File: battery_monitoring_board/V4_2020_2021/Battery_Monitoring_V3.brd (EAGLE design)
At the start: 57.1 x 161.5 mm, 97 parts, among them CON1 MOLEX_5566-2, CON2 SM03B-GHS-TB, CON3 SM03B-GHS-TB, J1 MKDS_5/2-6,352, J10 MKDS_5/2-6,352, J11 MKDS_5/2-6,352, J2 MKDS_5/2-6,352, J3 MKDS_5/2-6,352, J4 MKDS_5/2-6,352, J5 MKDS_5/2-6,352, J6 MKDS_5/2-6,352, J7 MKDS_5/2-6,352, J8 MKDS_5/2-6,352, J9 MKDS_5/2-6,352, Q1 TCLD1000CT, Q10 SI7145DP, Q11 SI7145DP, Q12 SI7145DP, Q13 SI7145DP, Q14 SI7145DP, Q15 PSMN1R5-30BLE, Q16 TCLD1000CT, Q2 TCLD1000CT, Q3 TCLD1000CT, Q4 PSMN1R5-30BLE, Q5 PSMN1R5-30BLE, Q6 PSMN1R5-30BLE, Q7 SI7145DP, Q8 SI7145DP, Q9 SI7145DP, U1 INA3221., U2 INA3221., U3 TEENSY_3.1_BASIC_2, U4 TCAN1042HVDR, U5 LTC4418

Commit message: started new sheet
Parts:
- added 3V3, DANGER: (no value), adafruit:1206
- added C13, C14, C15, C16: 0.01uF, adafruit:C0805
- added C17: 10uF, adafruit:C1206
- added C18: 1.5uF, adafruit:C0805
- added CON4: MOLEX_5566-2, ARVP:5566-2
- added D5: (no value), diode:DO-214AC
- added J12, J13, J14, J15, J16, J17: MKDS_5/2-6,352, Moira:MKDS_5/2-6,35
- added JP7: (no value), pinhead:1X02
- added Q17, Q18, Q19, Q20: NMOS-TO252, AlbertaSat:TO252
- added Q21: DMN2011UTS, Lydia:SOP65P640X120-8N
- added R39, R40: 240, resistor:R1206
- added R41, R42, R43, R44: 100k, adafruit:R1206
- added R45: 5.1, adafruit:R1206
- added R46: 1k, rcl:R0805
- added U10, U6, U7, U8: LM5050-2, AlbertaSat:MK06A
- added U12: IR2301S, Lydia:SOIC8
- added U9: TEENSY_3.1_BASIC_2, Teensy_3_Series_Board_v1.0:TEENSY_3.1_BASIC_2
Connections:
- new net +5V1: JP7.2
- new net GATE1: Q17.1, U6.5
- new net GATE2: Q18.1, U7.5
- new net GATE3: Q19.1, U8.5
- new net GATE4: Q20.1, U10.5
- new net GATE5: R46.1, U12.7
- new net IO1: U12.2, U9.10
- new net IO2: U10.3, U6.3, U7.3, U8.3, U9.6
- new net IO3: R42.1, U7.1, U9.8
- new net IO4: R41.1, U8.1, U9.5
- new net IO5: R43.1, U6.1, U9.9
- new net IO6: R44.1, U10.1, U9.7
- new net LEAK_IN: U9.14/A0
- new net LED_D: R39.1, U9.23/A9
- new net N$12: DANGER.A, R39.2
- new net N$13: C17.1, J15.2, Q21.5, Q21.6, Q21.7, Q21.8, R45.1, U12.1
- new net N$17: 3V3.A, R40.1
- new net N$18: C18.2, U12.6
- new net N$19: C18.1, D5.C, U12.8
- new net N$20: Q21.4, R46.2
- new net N$21: D5.A, R45.2
- new net VBATT1: C14.1, J14.2, Q17.3, U6.4
- new net VBATT2: C13.1, J13.2, Q18.3, U7.4
- new net VBATT3: C15.1, J12.2, Q19.3, U8.4
- new net VBATT4: C16.1, J17.2, Q20.3, U10.4
- new net VIN1: JP7.1
- new net VOUT: J16.1, Q17.2, Q18.2, Q19.2, Q20.2, Q21.1, Q21.2, Q21.3, U10.6, U6.6, U7.6, U8.6
- net +3V3: now also R40.2, U9.3.3V
- net +5V: now also CON4.1, R41.2, R42.2, R43.2, R44.2
- net AGND: now also U9.AGND
- net GND: now also 3V3.C, C13.2, C14.2, C15.2, C16.2, C17.2, CON4.2, DANGER.C, J12.1, J13.1, J14.1, J15.1, J16.2, J17.1, U10.2, U12.3, U12.4, U6.2, U7.2, U8.2, U9.GND
- net VIN: now also U9.VIN

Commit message: Removed duplicate teensy
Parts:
- removed 3V3, DANGER: (no value), adafruit:1206
- removed CON4: MOLEX_5566-2, ARVP:5566-2
- removed JP7: (no value), pinhead:1X02
- removed R39, R40: 240, resistor:R1206
- removed U9: TEENSY_3.1_BASIC_2, Teensy_3_Series_Board_v1.0:TEENSY_3.1_BASIC_2
- added 3V1, DANGER1: (no value), adafruit:1206
- added R36, R37: 240, resistor:R1206
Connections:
- removed net +5V1: JP7.2
- removed net N$12: DANGER.A, R39.2
- removed net N$17: 3V3.A, R40.1
- removed net VIN1: JP7.1
- new net N$22: 3V1.A, R37.1
- new net N$23: DANGER1.A, R36.2
- net +3V3: now also R37.2; no longer R40.2, U9.3.3V
- net +5V: no longer CON4.1
- net AGND: no longer U9.AGND
- net GND: now also 3V1.C, DANGER1.C; no longer 3V3.C, CON4.2, DANGER.C, U9.GND
- net IO1: now also U3.17/A3; no longer U9.10
- net IO2: now also U3.13; no longer U9.6
- net IO3: now also U3.15/A1; no longer U9.8
- net IO4: now also U3.12; no longer U9.5
- net IO5: now also U3.16/A2; no longer U9.9
- net IO6: now also U3.14/A0; no longer U9.7
- net LEAK_IN: now also U3.11; no longer U9.14/A0
- net LED_D: now also R36.1, U3.23/A9; no longer R39.1, U9.23/A9
- net VIN: no longer U9.VIN

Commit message: Removed jumpers
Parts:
- removed J11, J12, J13, J14, J15, J17, J5, J6, J7, J8: MKDS_5/2-6,352, Moira:MKDS_5/2-6,35
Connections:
- removed net LEAK_IN: U3.11
- removed net N$13: C17.1, J15.2, Q21.5, Q21.6, Q21.7, Q21.8, R45.1, U12.1
- removed net VBATT1: C14.1, J14.2, Q17.3, U6.4
- removed net VBATT2: C13.1, J13.2, Q18.3, U7.4
- removed net VBATT3: C15.1, J12.2, Q19.3, U8.4
- removed net VBATT4: C16.1, J17.2, Q20.3, U10.4
- net ELECTRONICS_BATTERY: now also C17.1, Q21.5, Q21.6, Q21.7, Q21.8, R45.1, U12.1
- net GND: no longer J11.2, J12.1, J13.1, J14.1, J15.1, J17.1, J5.2, J6.2, J7.2, J8.2
- net MOTOR1: now also C14.1, Q17.3, U6.4; no longer J5.1
- net MOTOR2: now also C13.1, Q18.3, U7.4; no longer J6.1
- net MOTOR3: now also C15.1, Q19.3, U8.4; no longer J7.1
- net MOTOR4: now also C16.1, Q20.3, U10.4; no longer J11.1
- net POWER_BOARD: no longer J8.1
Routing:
- net MOTOR4: track 127.8 -> 121.9 mm

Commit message: started work on PCB layout
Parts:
- moved Q17 129.3 mm to (-15.0, 65.4), turned to 270 degrees
- moved Q19 124.6 mm to (8.76, 60.8), turned to 270 degrees
- moved Q18 111.7 mm to (9.27, 48.9), turned to 270 degrees
- moved Q20 106.1 mm to (-15.6, 30.1), turned to 270 degrees
- moved J16 77.4 mm to (-16.8, 15.5), turned to 270 degrees
- moved C13 49.7 mm to (37.6, -32.8)
- moved C14 49.7 mm to (44.8, -32.8)
- moved C15 49.7 mm to (52.1, -32.8)
- moved C16 49.7 mm to (59.3, -32.8)
- moved C18 49.7 mm to (-0.13, -39.0)
- moved R36 49.7 mm to (0.25, -63.0)
- moved R37 49.7 mm to (5.33, -63.0)
- moved R46 49.7 mm to (45.1, -22.2)
- moved U10 49.7 mm to (52.5, -38.9)
- moved U6 49.7 mm to (34.5, -38.9)
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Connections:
- net ELECTRONICS_BATTERY: no longer C17.1, Q21.5, Q21.6, Q21.7, Q21.8, R45.1, U12.1
- net POWER_BOARD: now also C17.1, Q21.5, Q21.6, Q21.7, Q21.8, R45.1, U12.1
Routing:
- net MOTOR2: track 121.2 -> 93.3 mm
- net MOTOR3: track 107.7 -> 104.1 mm
- net BATTERY_3: track 149.7 -> 147.0 mm
- net BATTERY_2: track 128.0 -> 127.4 mm

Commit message: slight positioning changes
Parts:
- moved Q17 33.0 mm to (9.27, 43.0)
- moved Q20 25.4 mm to (9.65, 27.6)
- moved Q7 12.3 mm to (33.3, 57.3)
- moved Q9 12.1 mm to (32.4, 43.2)
- moved R8 12.0 mm to (22.2, 43.1)
- moved R35 10.6 mm to (22.2, 27.7)
- moved C2 8.81 mm to (17.1, 135.2)
- moved ARVP1 8.81 mm to (9.53, 109.8)
- moved C1 8.81 mm to (15.9, 145.3)
- moved C10 8.81 mm to (3.17, 100.9)
- moved C3 8.81 mm to (43.5, 139.5)
- moved C4 8.81 mm to (36.4, 143.4)
- moved C5 8.81 mm to (13.3, 92.0)
- moved C6 8.81 mm to (8.26, 92.0)
- moved C7 8.81 mm to (4.45, 92.0)
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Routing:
- net BATTERY_4: track 173.6 -> 138.1 mm
- net MOTOR1: track 143.0 -> 116.7 mm
- net BATTERY_5: track 146.4 -> 135.8 mm
- net N$6: track 10.9 -> 2.86 mm
- net +3V3: track 123.6 -> 118.2 mm
- net SDA: track 80.4 -> 75.9 mm
- net SCL: track 69.3 -> 64.8 mm
- net MOTOR4: track 121.9 -> 120.5 mm
- net N$9: track 10.9 -> 9.55 mm

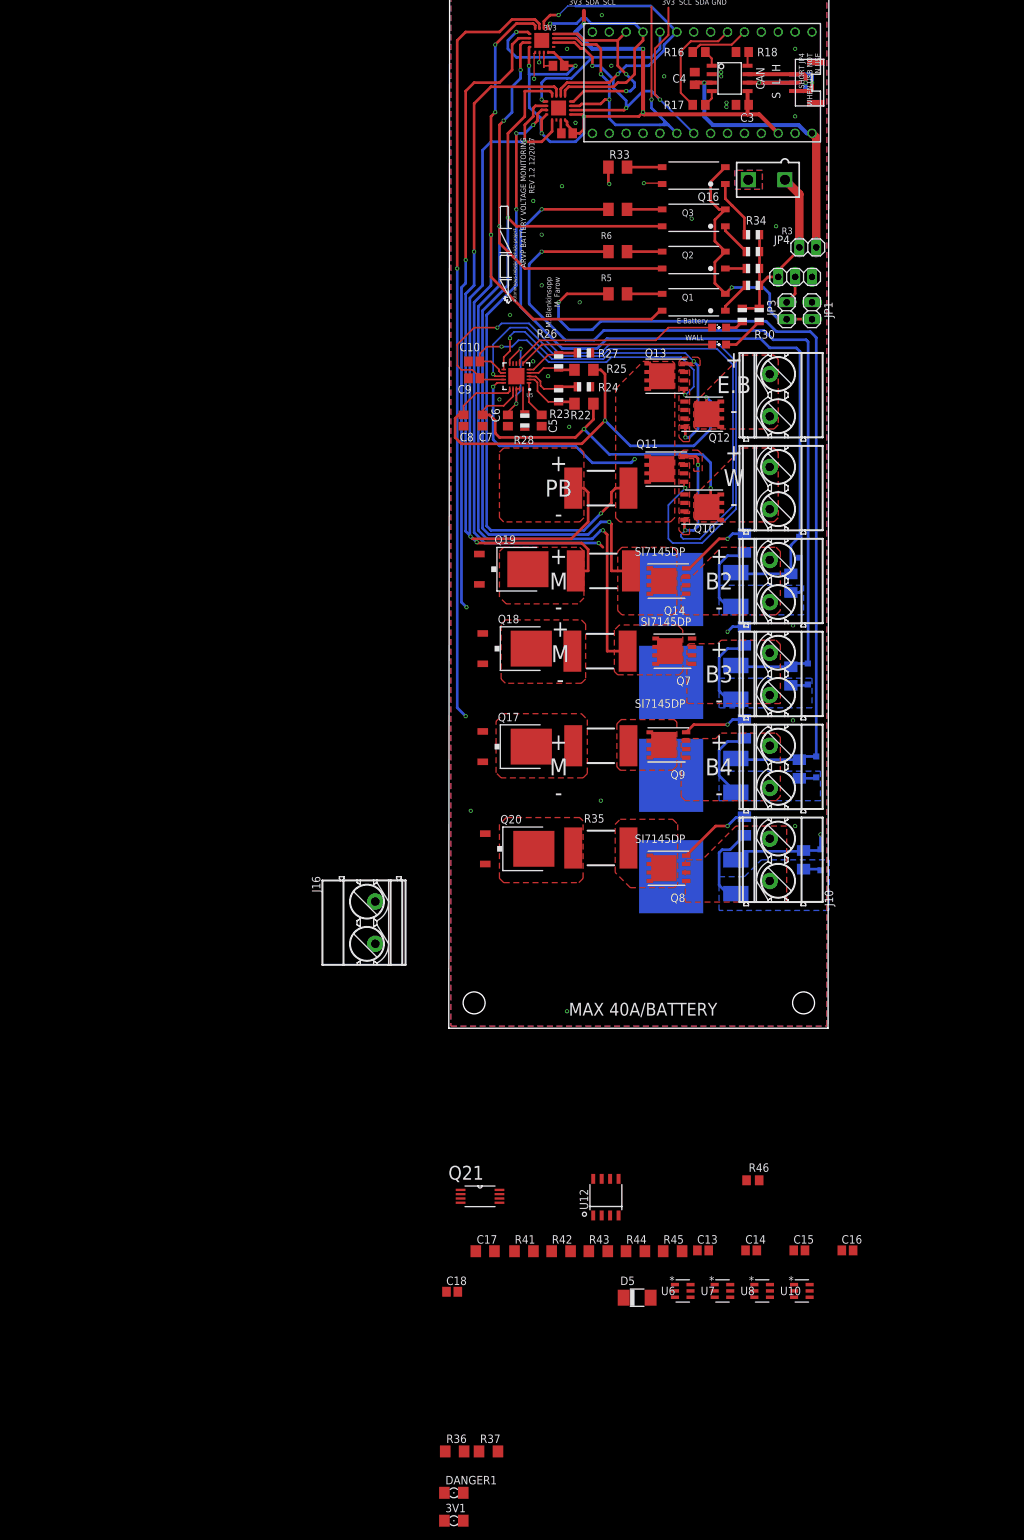
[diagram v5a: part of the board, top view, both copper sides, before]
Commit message: adjusting the resistor, capacitor, and ic positions
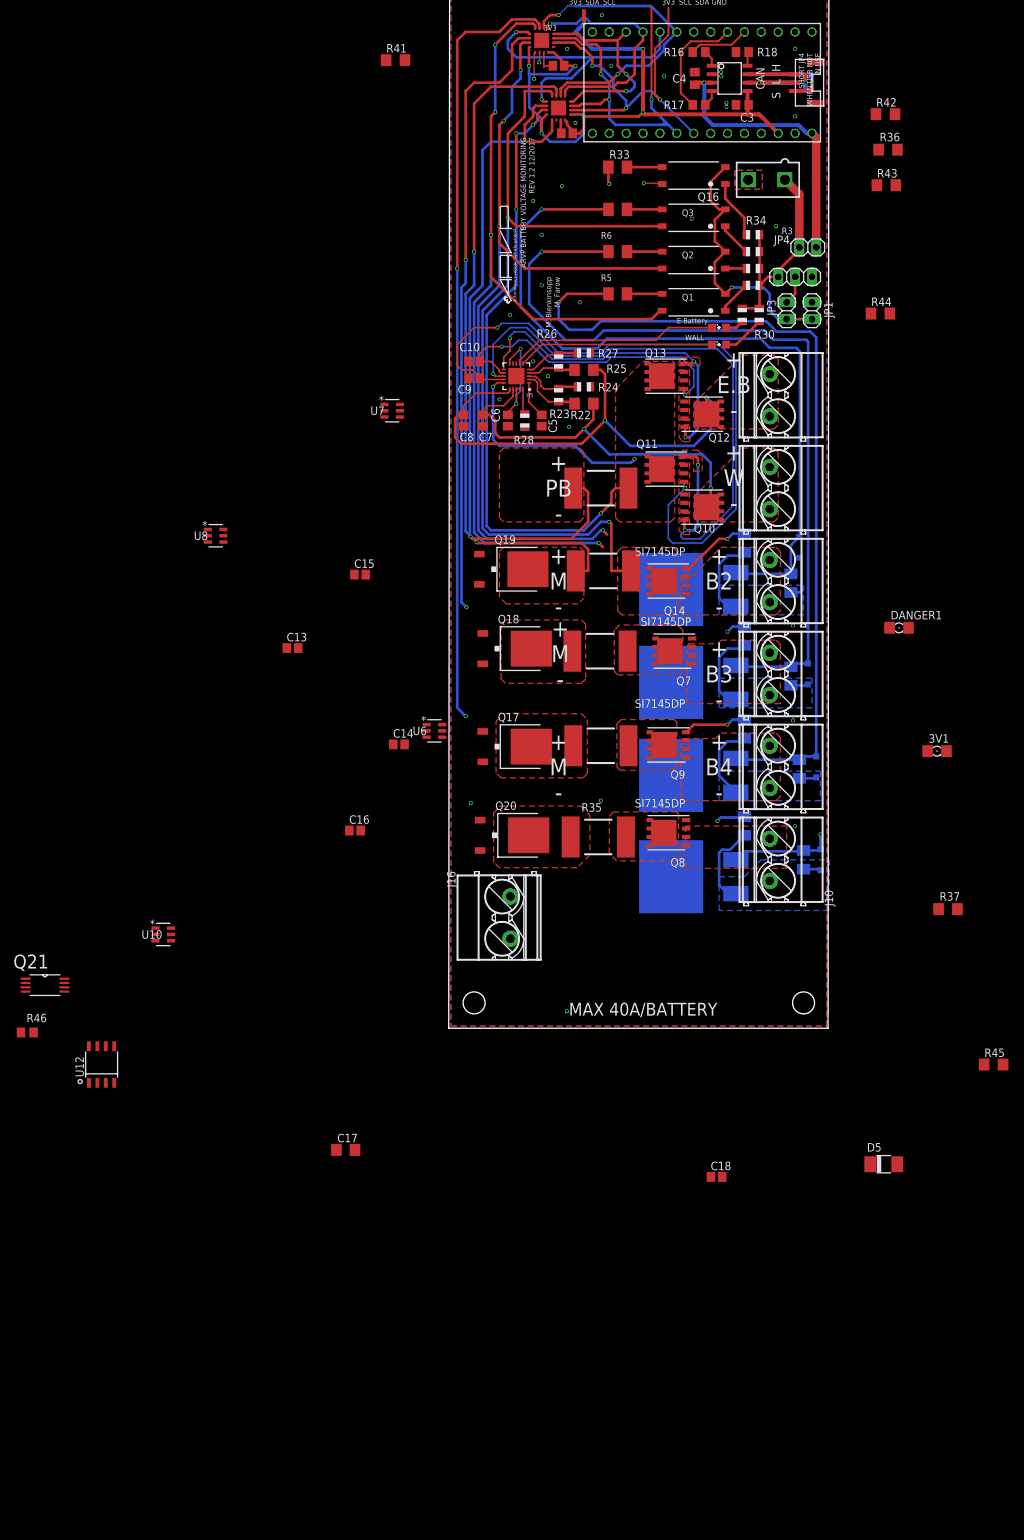
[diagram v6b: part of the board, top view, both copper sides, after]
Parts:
- moved R36 206.3 mm to (65.4, 132.7)
- moved R41 180.1 mm to (-8.64, 146.2)
- moved R42 177.8 mm to (65.0, 138.0)
- moved R43 166.0 mm to (65.2, 127.4)
- moved DANGER1 146.3 mm to (67.1, 60.8)
- moved R44 145.7 mm to (64.3, 108.1)
- moved U7 141.3 mm to (-9.14, 93.5)
- moved U8 140.2 mm to (-35.7, 74.7)
- moved 3V1 136.6 mm to (72.8, 42.3)
- moved C15 121.2 mm to (-14.0, 68.8)
- moved R46 111.3 mm to (-64.0, 0.00)
- moved U10 110.0 mm to (-43.6, 14.7)
- moved C13 109.6 mm to (-24.1, 57.8)
- moved R37 106.9 mm to (74.4, 18.5)
- moved C16 97.3 mm to (-14.7, 30.4)
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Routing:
- net BATTERY_3: track 147.0 -> 126.4 mm
- net N$10: track 11.1 -> 4.27 mm
- net MOTOR4: track 120.5 -> 119.4 mm

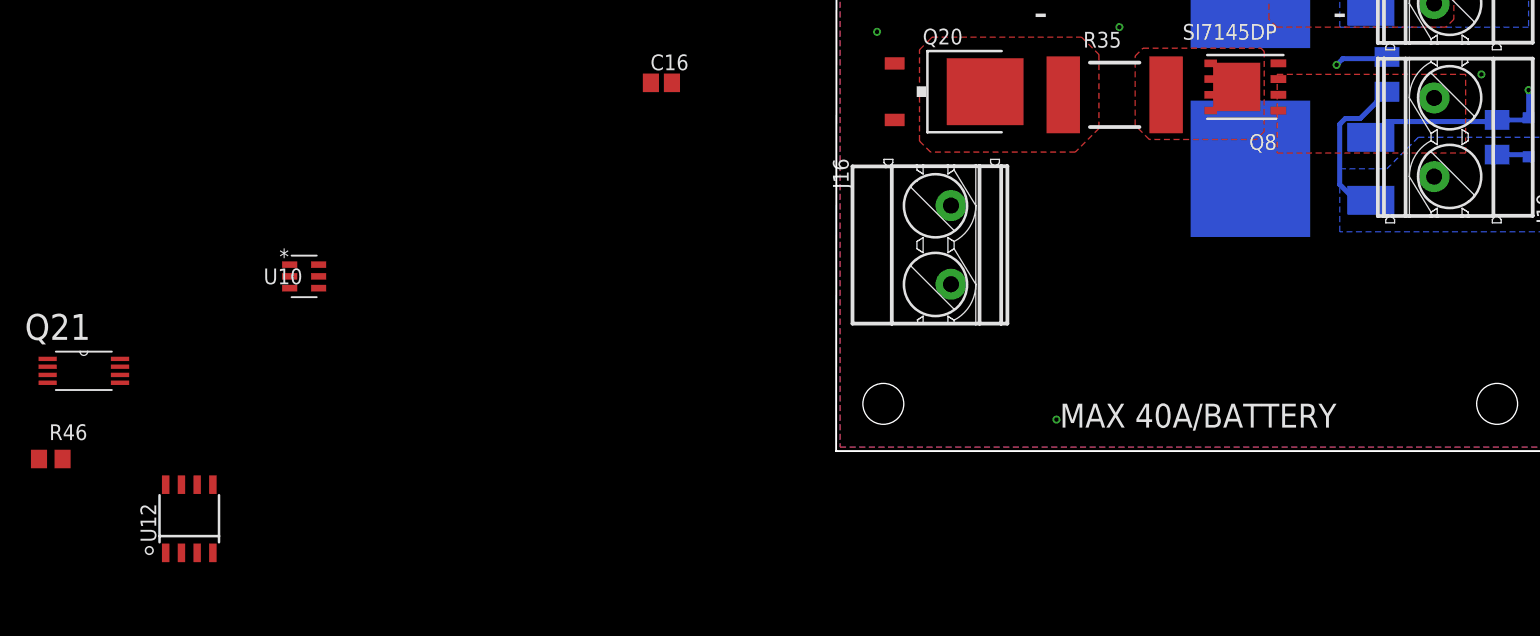
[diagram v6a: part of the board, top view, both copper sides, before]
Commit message: minor component location changes
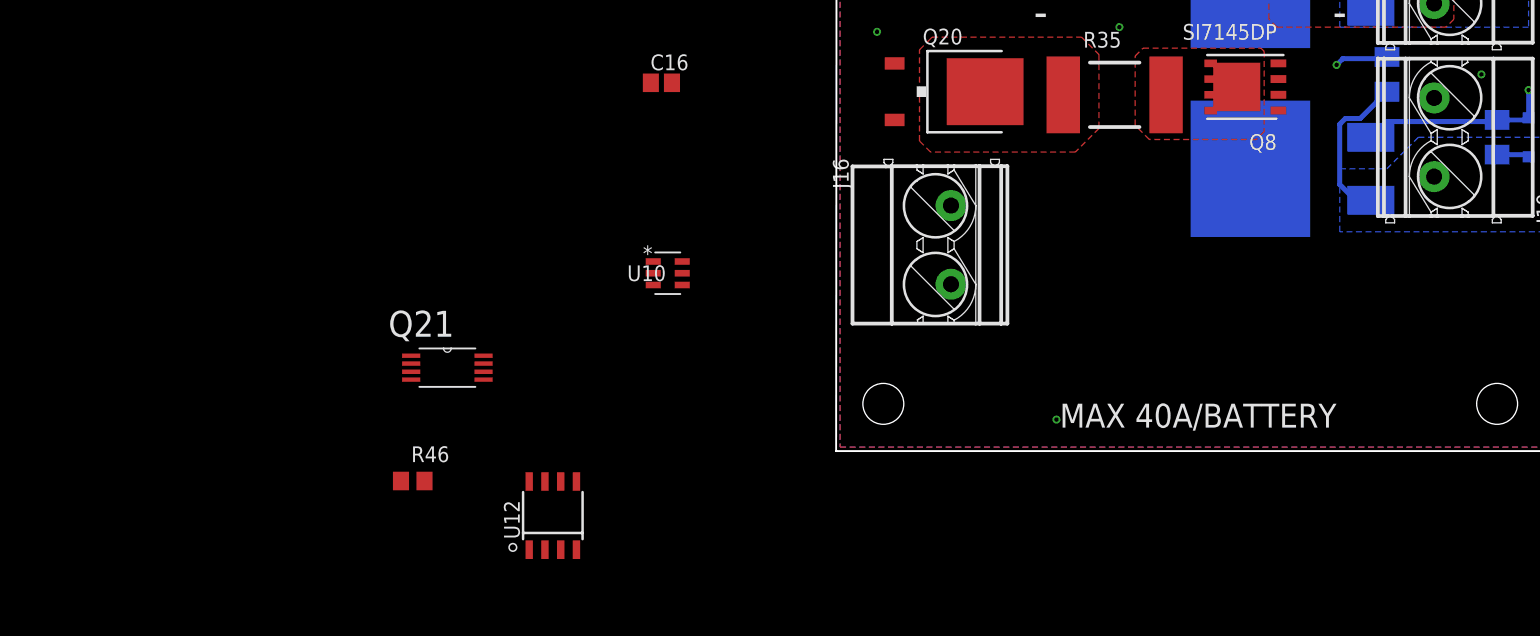
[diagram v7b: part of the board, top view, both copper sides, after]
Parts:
- moved Q21 29.3 mm to (-32.0, 7.37)
- moved U10 29.3 mm to (-14.2, 15.0)
- moved U12 29.3 mm to (-23.5, -4.57)
- moved R46 29.3 mm to (-34.8, -1.78)
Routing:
- removed copper zone on layer 1, net BATTERY5_IN
